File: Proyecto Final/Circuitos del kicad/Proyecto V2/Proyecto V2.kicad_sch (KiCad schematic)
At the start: 43 parts, among them J1 12v, Q1 PN2222A, Q2 PN2222A, Q3 PN2222A, SW1 SW_Push, SW2 SW_Push, SW3 SW_Push, SW4 SW_Push, U1 LM7805, U3 ATmega328P-P, Y1 16MHz

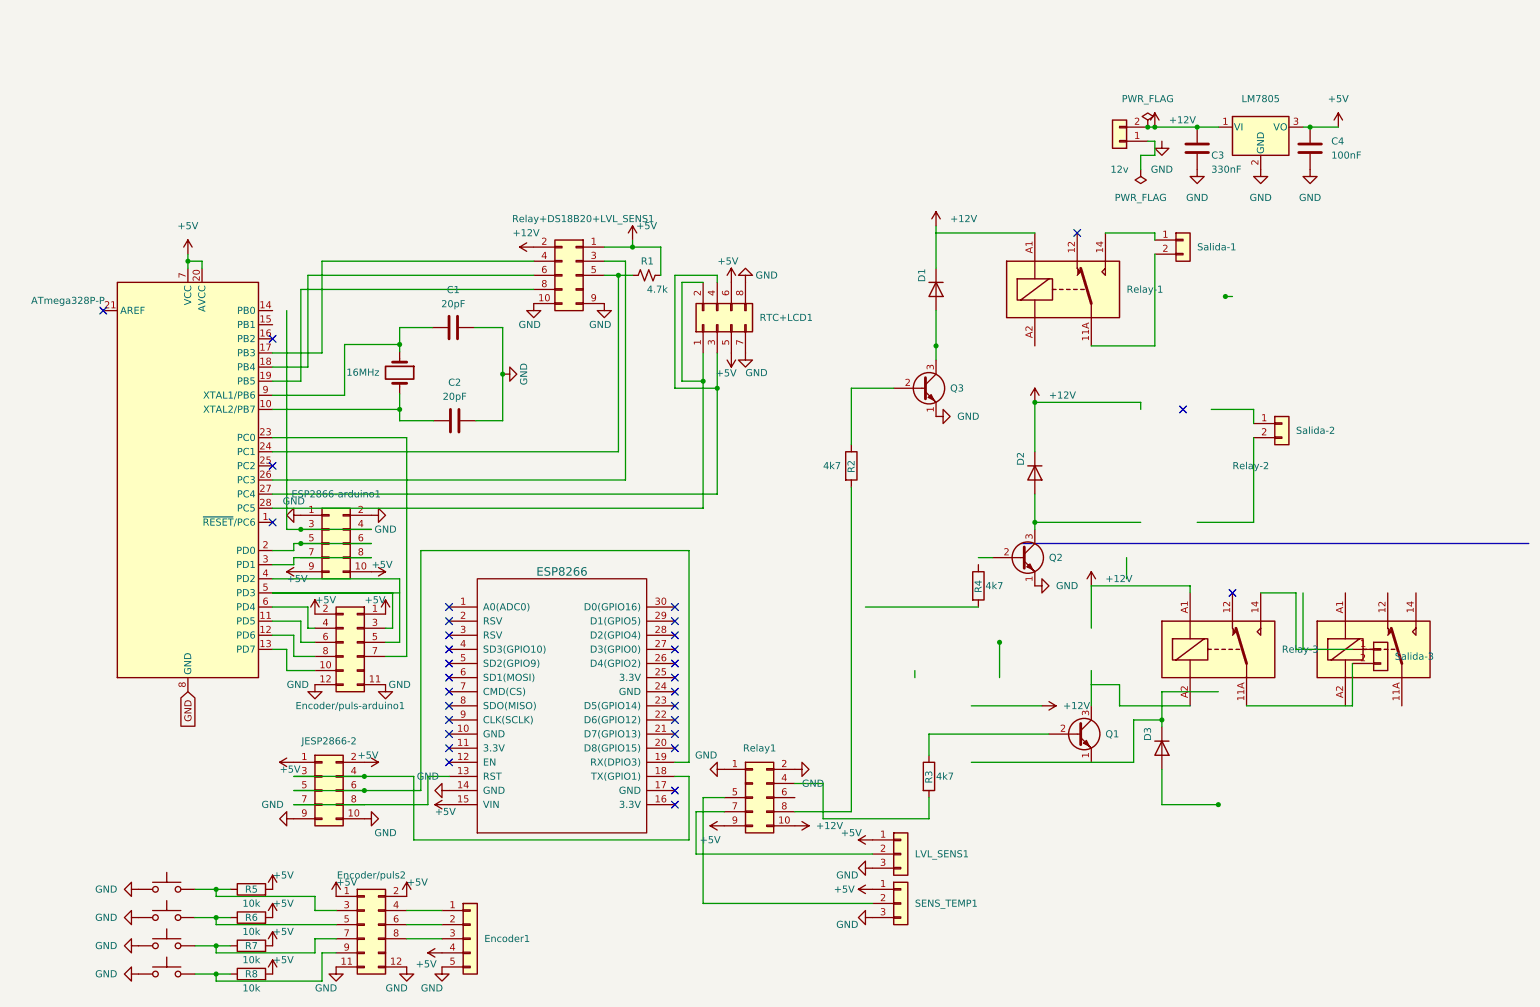
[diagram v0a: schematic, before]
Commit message: Arreglo derrame del kicad
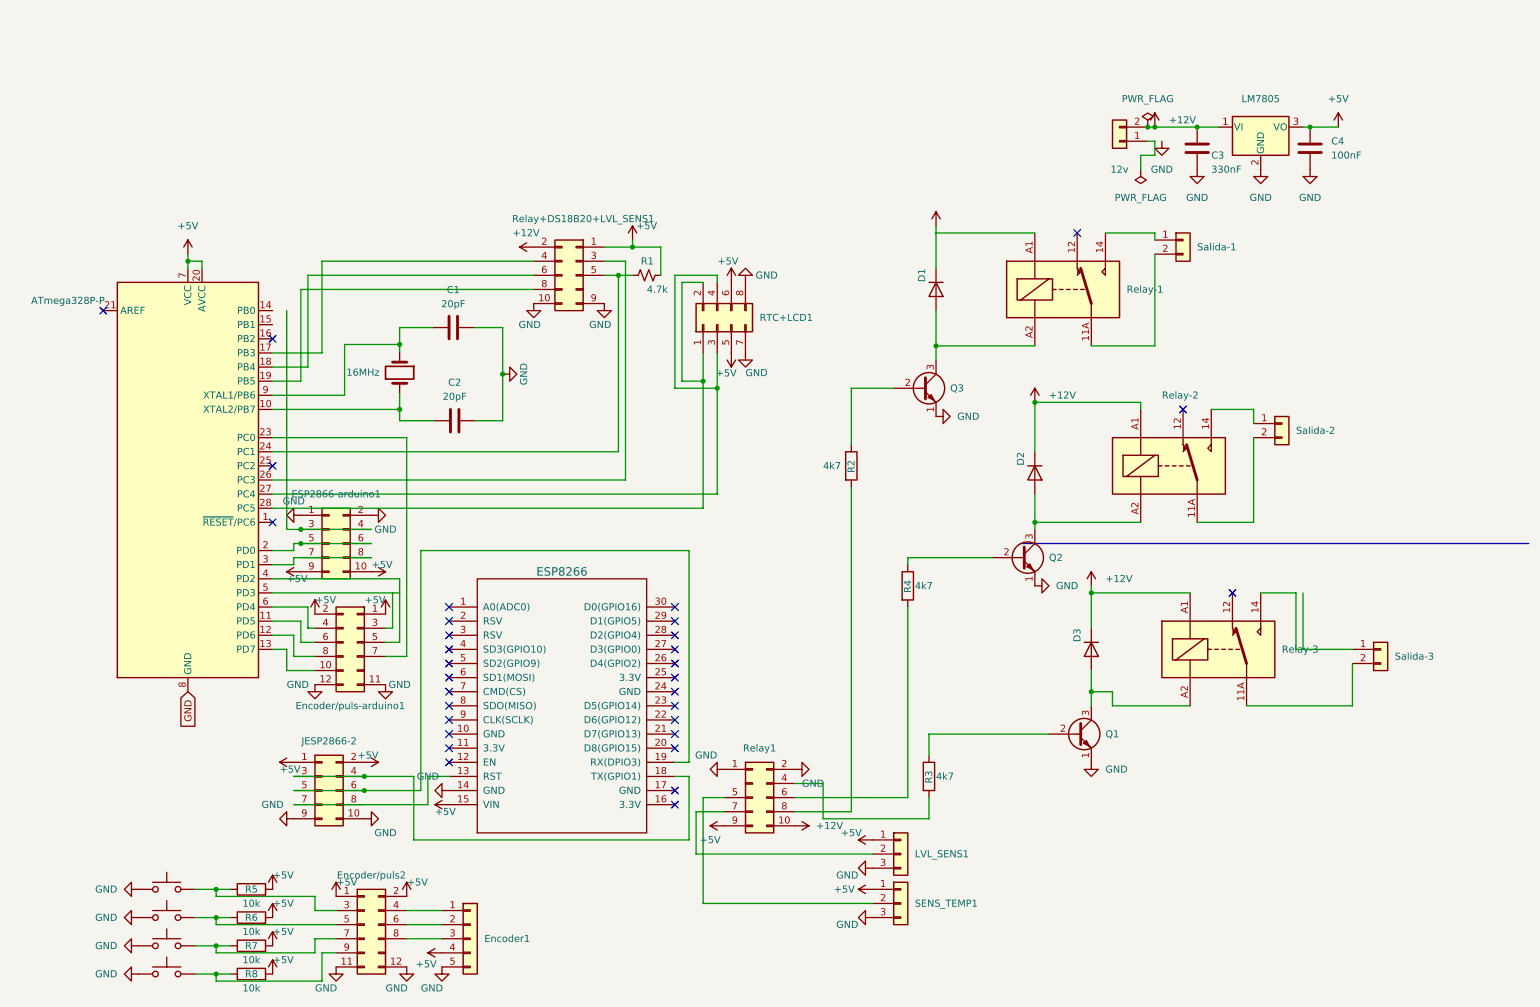
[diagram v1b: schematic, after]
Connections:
- net +12V: now also D3.1 (K), Relay-2.A1
- net GND: now also Q1.1 (E)
- net at D1.2 (A), Q3.3 (C): now also Relay-1.A2
- net at D3.2 (A): now also Q1.3 (C), Relay-3.A2
- net at Salida-2.1 (Pin_1): now also Relay-2.14
- net at Salida-2.2 (Pin_2): now also Relay-2.11A, Relay-2.11B
- net at Relay-2.A2: now also D2.2 (A), Q2.3 (C)
- net at Relay1.6 (Pin_6): now also R4.2
- net at R4.1: now also Q2.2 (B)
- net at U3.5 (PD3): no longer Encoder/puls-arduino1.3 (Pin_3)
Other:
- moved on the sheet: D3, R4, Relay-2

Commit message: Agora sem
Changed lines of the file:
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@@
-    (stroke (width 0) (type default) (color 0 0 0 0))
-  )
-  (wire (pts (xy 245.11 128.27) (xy 245.11 118.11))
     (stroke (width 0) (type default) (color 0 0 0 0))
   )
@@
       (effects (font (size 1.27 1.27)) hide)
     )
-    (property "Value" "" (id 1) (at 181.61 50.7999 0)
+    (property "Value" "+12V" (id 1) (at 181.61 50.7999 0)
       (effects (font (size 1.27 1.27)) (justify left))
     )

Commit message: a
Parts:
- removed ESP2866-arduino1, JESP2866-2: Conn_02x05_Odd_Even, Connector_IDC:IDC-Header_2x05_P2.54mm_Vertical, symbol Connector_Generic:Conn_02x05_Odd_Even
- removed ESP8266: NodeMCU1.0(ESP-12E), ESP8266 LOLiN v3:ESP8266, symbol ESP8266-2:NodeMCU1.0(ESP-12E)
- added C5: 100nF, Capacitor_THT:C_Disc_D5.0mm_W2.5mm_P5.00mm, symbol Device:C
- added C6: 10uF, Capacitor_THT:C_Disc_D5.0mm_W2.5mm_P5.00mm, symbol Device:C
- added U2: ESP-12E, ESP8266-12E_ESP-12E:XCVR_ESP8266-12E_ESP-12E, symbol ESP8266:ESP-12E
- added U4: LD1117S33TR_SOT223, Package_TO_SOT_THT:TO-220-3_Vertical, symbol Regulator_Linear:LD1117S33TR_SOT223
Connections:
- net +5V: now also C5.1, U4.3 (VI)
- net GND: now also J1.1 (Pin_1), C5.2, C6.2, U2.9 (GND), U4.1 (GND)
- net at U3.14 (PB0): now also U2.1 (REST)
- net at U3.2 (PD0): now also U2.15 (RXD)
- net at U3.3 (PD1): now also U2.16 (TXD)
- new net: C6.1, U2.8 (VCC), U4.2 (VO)
- no-connect marks 32 -> 24

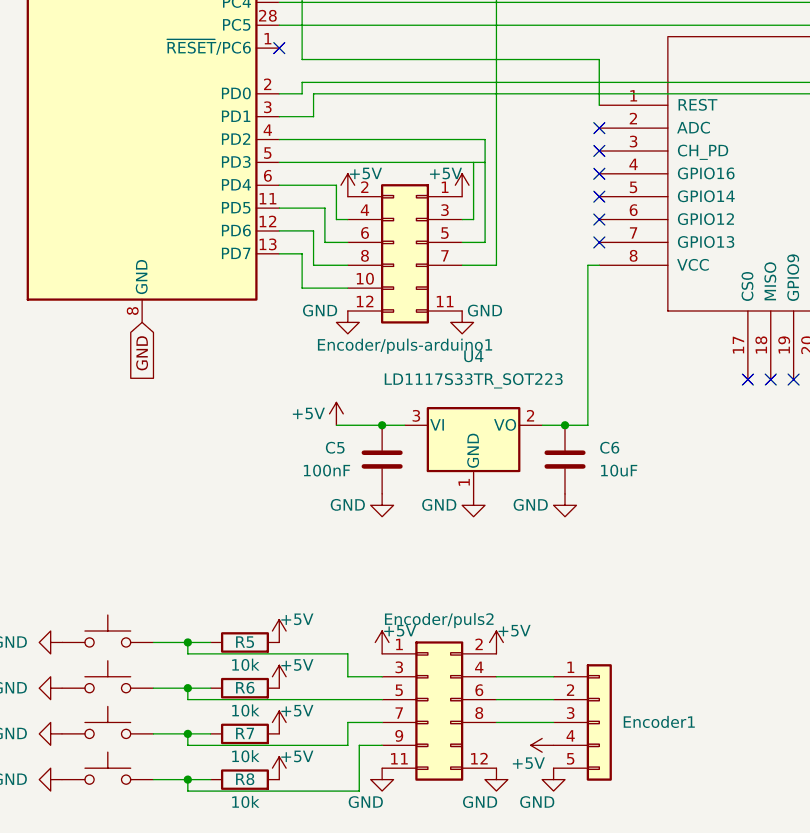
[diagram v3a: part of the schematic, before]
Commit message: Cambios ESP y pines
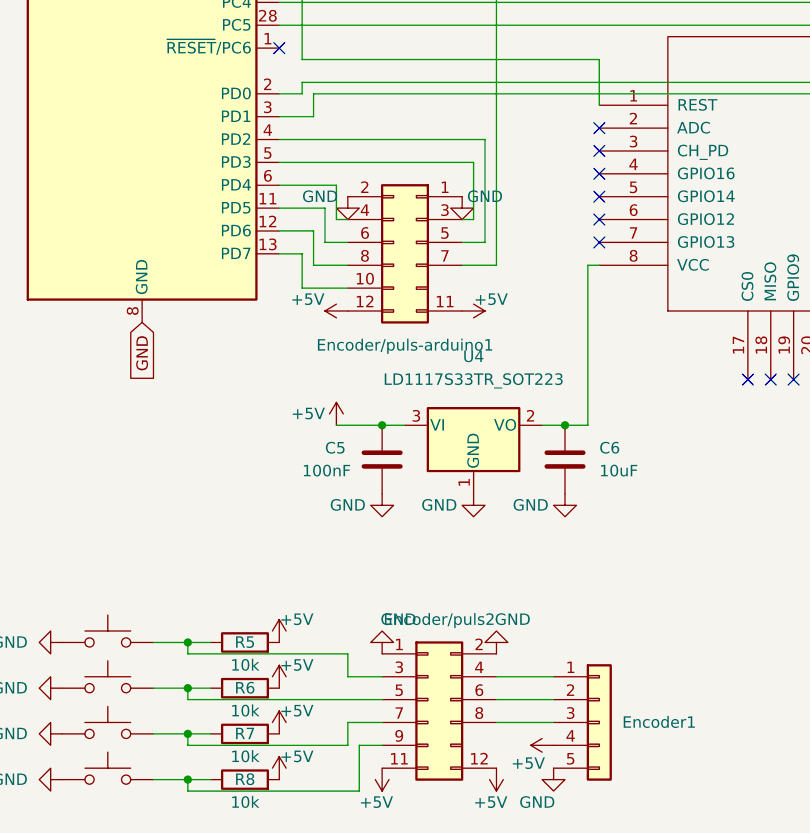
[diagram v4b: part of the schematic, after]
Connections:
- net +5V: now also Encoder/puls-arduino1.11 (Pin_11), Encoder/puls-arduino1.12 (Pin_12), Encoder/puls2.11 (Pin_11), Encoder/puls2.12 (Pin_12); no longer Encoder/puls-arduino1.1 (Pin_1), Encoder/puls-arduino1.2 (Pin_2), Encoder/puls2.1 (Pin_1), Encoder/puls2.2 (Pin_2)
- net GND: now also Encoder/puls-arduino1.1 (Pin_1), Encoder/puls-arduino1.2 (Pin_2), Encoder/puls2.1 (Pin_1), Encoder/puls2.2 (Pin_2); no longer Encoder/puls-arduino1.11 (Pin_11), Encoder/puls-arduino1.12 (Pin_12), Encoder/puls2.11 (Pin_11), Encoder/puls2.12 (Pin_12)
- net at U3.5 (PD3): now also Encoder/puls-arduino1.3 (Pin_3)

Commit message: Cositas ricas en kikiriki
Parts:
- added J2, J3: Conn_01x05, Connector_PinHeader_2.54mm:PinHeader_1x05_P2.54mm_Vertical, symbol Connector_Generic:Conn_01x05
- added J4, J5: Conn_01x08, Connector_PinHeader_2.54mm:PinHeader_1x08_P2.54mm_Vertical, symbol Connector_Generic:Conn_01x08
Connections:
- net +5V: now also J2.5 (Pin_5); no longer C5.1, U4.3 (VI)
- net GND: now also J2.1 (Pin_1), J3.1 (Pin_1); no longer U2.9 (GND)
- net at C6.1, U2.8 (VCC), U4.2 (VO): now also J4.8 (Pin_8)
- net at U2.1 (REST): now also J3.4 (Pin_4), J4.1 (Pin_1); no longer U3.14 (PB0)
- net at U2.15 (RXD): now also J3.2 (Pin_2), J5.2 (Pin_2); no longer U3.2 (PD0)
- net at U2.16 (TXD): now also J3.3 (Pin_3), J5.1 (Pin_1); no longer U3.3 (PD1)
- net at U2.10 (GPIO15): now also J5.7 (Pin_7)
- net at U2.11 (GPIO2): now also J5.6 (Pin_6)
- net at U2.12 (GPIO0): now also J5.5 (Pin_5)
- net at U2.13 (GPIO4): now also J5.4 (Pin_4)
- net at U2.14 (GPIO5): now also J5.3 (Pin_3)
- net at U2.2 (ADC): now also J4.2 (Pin_2)
- net at U2.3 (CH_PD): now also J4.3 (Pin_3)
- net at U2.4 (GPIO16): now also J4.4 (Pin_4)
- net at U2.5 (GPIO14): now also J4.5 (Pin_5)
- net at U2.6 (GPIO12): now also J4.6 (Pin_6)
- net at U2.7 (GPIO13): now also J4.7 (Pin_7)
- new net: J5.8 (Pin_8), U2.9 (GND)
- new net: C5.1, J3.5 (Pin_5), U4.3 (VI)
- new net: J2.2 (Pin_2), U3.2 (PD0)
- new net: J2.3 (Pin_3), U3.3 (PD1)
- new net: J2.4 (Pin_4), U3.14 (PB0)
- no-connect marks 24 -> 13
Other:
- note added: "RST"
- note added: "RX"
- note added: "TX"
- moved on the sheet: C1, C2, C5, C6, Encoder/puls-arduino1, R1, RTC+LCD1, Relay+DS18B20+LVL_SENS1, U2, U4

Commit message: Cambios varios
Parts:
- removed J2, J3: Conn_01x05, Connector_PinHeader_2.54mm:PinHeader_1x05_P2.54mm_Vertical, symbol Connector_Generic:Conn_01x05
- added J6: Conn_01x06, Connector_PinHeader_2.54mm:PinHeader_1x06_P2.54mm_Vertical, symbol Connector_Generic:Conn_01x06
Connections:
- net +5V: now also C5.1, U4.3 (VI)
- net GND: now also J5.8 (Pin_8), U2.9 (GND)
- net at J5.1 (Pin_1), U2.16 (TXD): now also U3.3 (PD1)
- net at J5.2 (Pin_2), U2.15 (RXD): now also U3.2 (PD0)
- net at J4.1 (Pin_1), U2.1 (REST): now also U3.14 (PB0)
- net at U2.17 (CS0): now also J6.6 (Pin_6)
- net at U2.18 (MISO): now also J6.5 (Pin_5)
- net at U2.19 (GPIO9): now also J6.4 (Pin_4)
- net at U2.20 (GPIO10): now also J6.3 (Pin_3)
- net at U2.21 (MOSI): now also J6.2 (Pin_2)
- net at U2.22 (SCLK): now also J6.1 (Pin_1)
- no-connect marks 13 -> 7

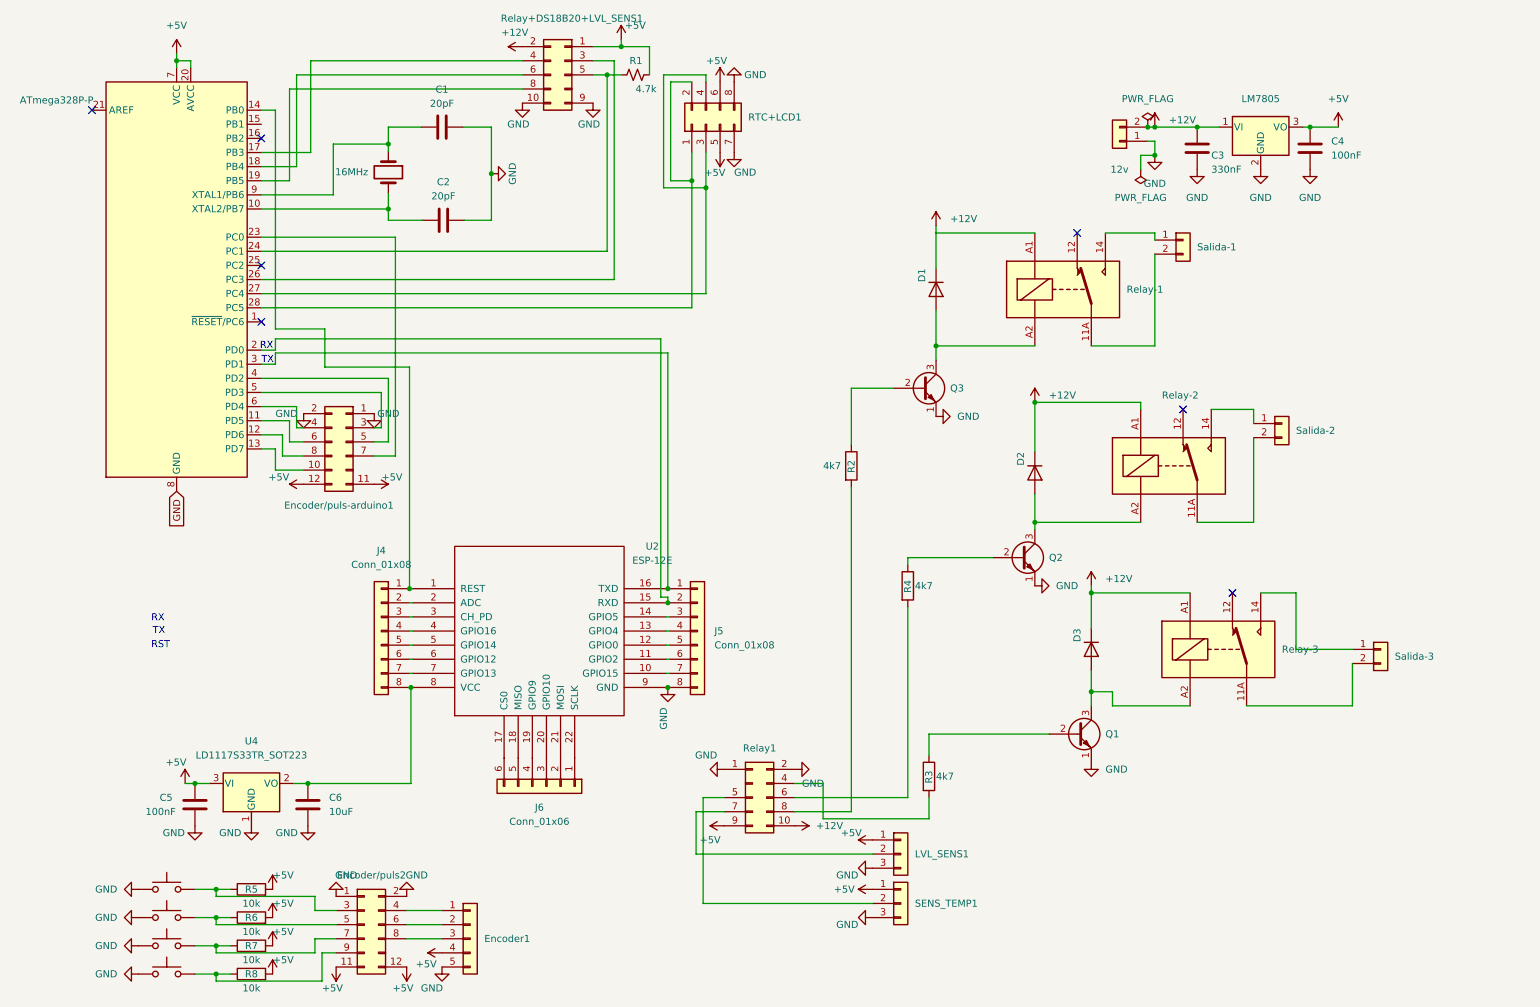
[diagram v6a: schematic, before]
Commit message: Agregado lib conversor y agregado a placa main
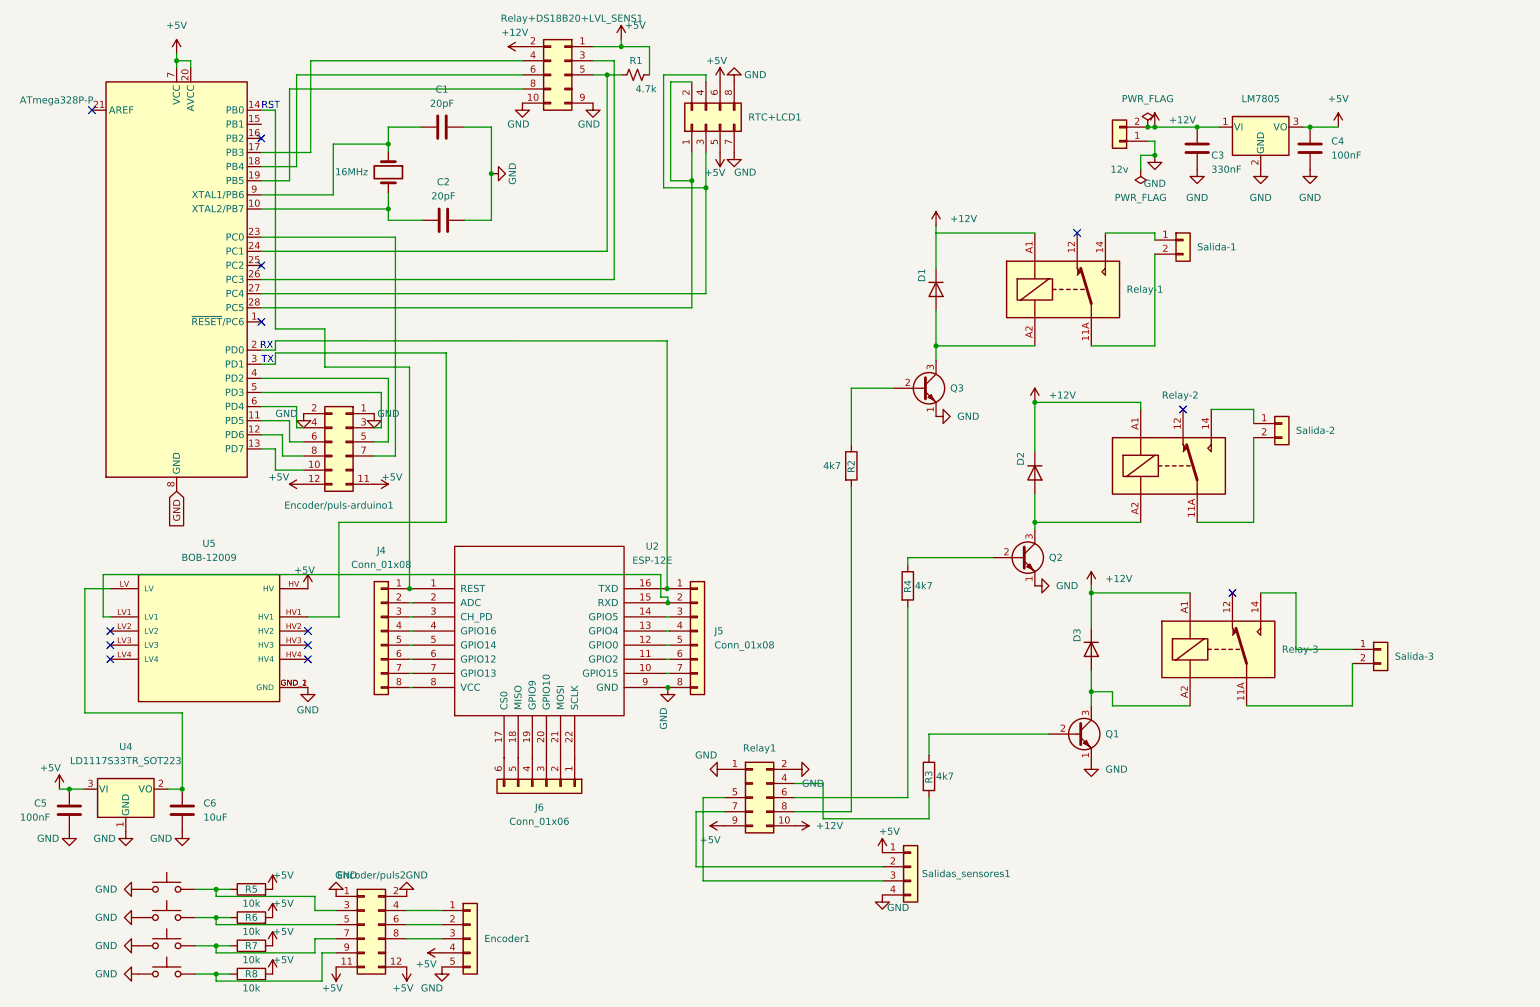
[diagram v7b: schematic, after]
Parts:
- removed LVL_SENS1, SENS_TEMP1: Conn_01x03, TerminalBlock:TerminalBlock_bornier-3_P5.08mm, symbol Connector_Generic:Conn_01x03
- added Salidas_sensores1: Conn_01x04, TerminalBlock:TerminalBlock_bornier-4_P5.08mm, symbol Connector_Generic:Conn_01x04
- added U5: BOB-12009, CONV_BOB-12009, symbol BOB-12009:BOB-12009
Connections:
- net +5V: now also Salidas_sensores1.1 (Pin_1), U5.HV
- net GND: now also Salidas_sensores1.4 (Pin_4), U5.GND_1 (GND), U5.GND_2 (GND)
- net at Relay1.5 (Pin_5): now also Salidas_sensores1.3 (Pin_3)
- net at J5.1 (Pin_1), U2.16 (TXD): now also U3.2 (PD0); no longer U3.3 (PD1)
- net at J5.2 (Pin_2), U2.15 (RXD): now also U5.LV1; no longer U3.2 (PD0)
- net at Relay1.7 (Pin_7): now also Salidas_sensores1.2 (Pin_2)
- net at C6.1, U4.2 (VO): now also U5.LV; no longer J4.8 (Pin_8), U2.8 (VCC)
- new net: U3.3 (PD1), U5.HV1
- new net: J4.8 (Pin_8), U2.8 (VCC)
- no-connect marks 7 -> 13
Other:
- moved on the sheet: C5, C6, U4
